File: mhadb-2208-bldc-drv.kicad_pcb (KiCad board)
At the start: 2 copper layers, 45 x 40 mm, 69 parts, among them J1 TC2030, J2 Conn_01x04, J3 Conn_01x04_Pin, M1 Motor_3_Phases, SW1 SW_Push, SW2 SW_Push, SW3 SW_Push, U1 SN65HVD230, U2 STM32F103C8Tx, U3 DRV8311H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

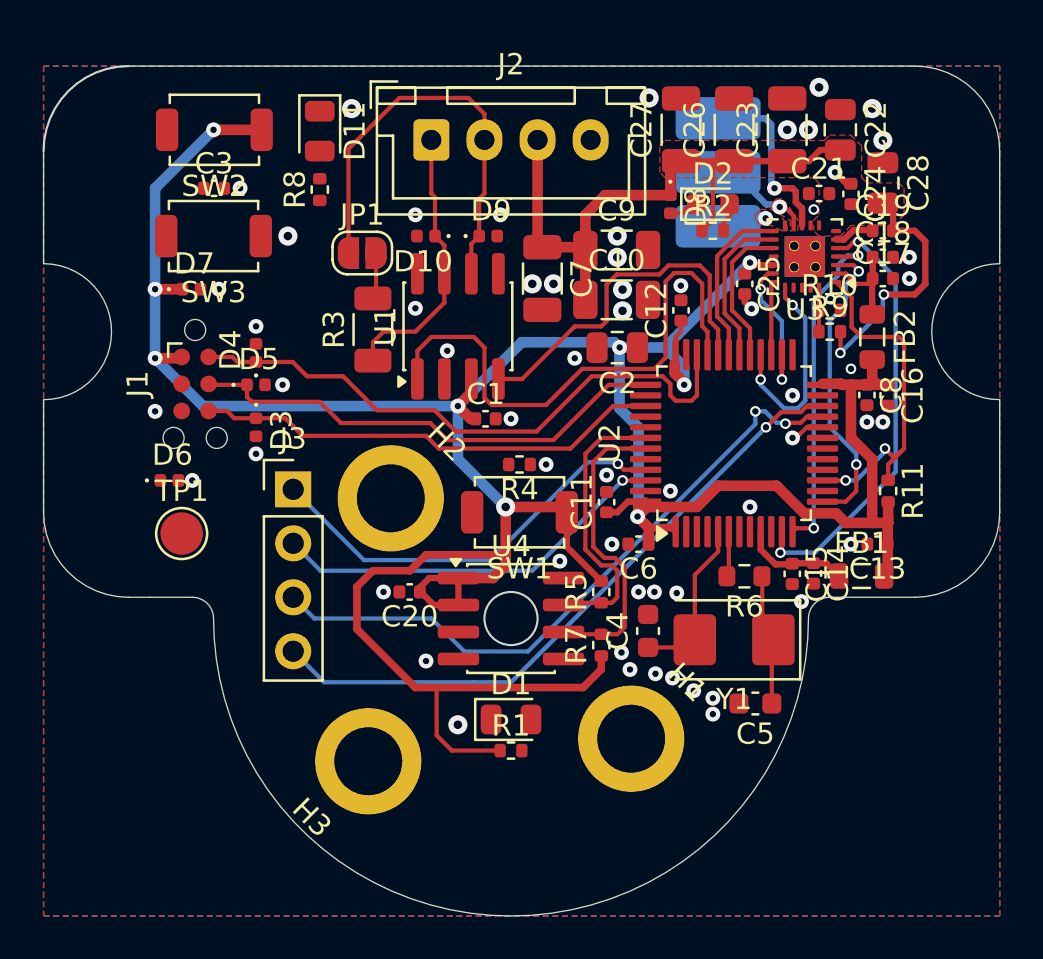
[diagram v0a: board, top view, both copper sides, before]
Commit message: pcb: route BOOT and RST
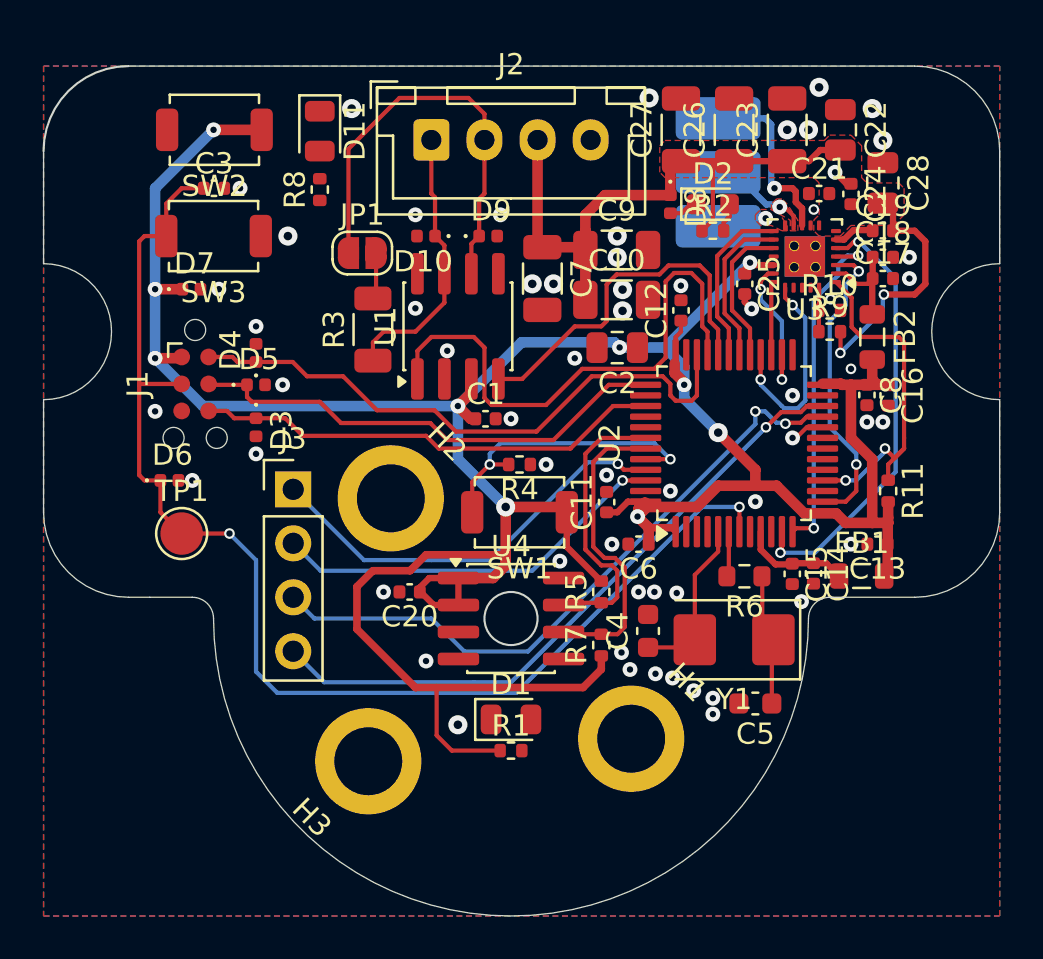
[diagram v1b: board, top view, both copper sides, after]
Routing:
- net /NRST: track 0.00 -> 59.2 mm, vias 0 -> 2
- net /BOOT: track 0.00 -> 14.2 mm, vias 0 -> 2
- net +3V3: track 152.4 -> 150.3 mm, vias 9 -> 10

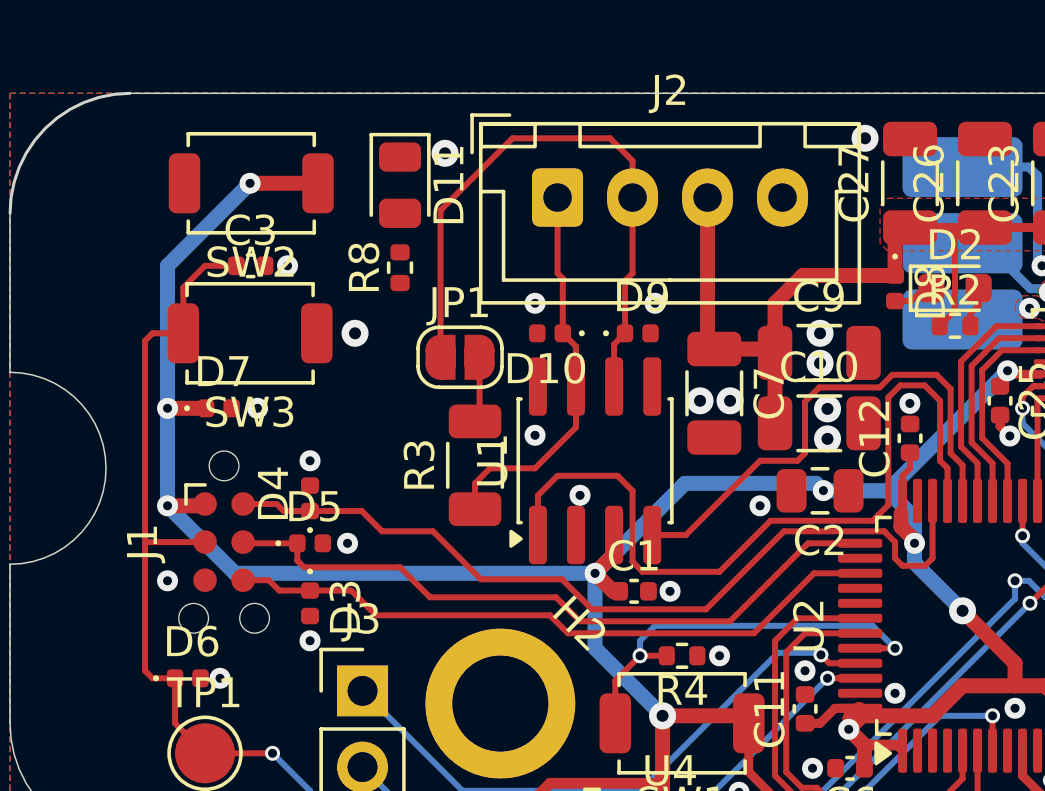
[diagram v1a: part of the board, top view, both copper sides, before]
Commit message: pcb: route BTN and CAN status
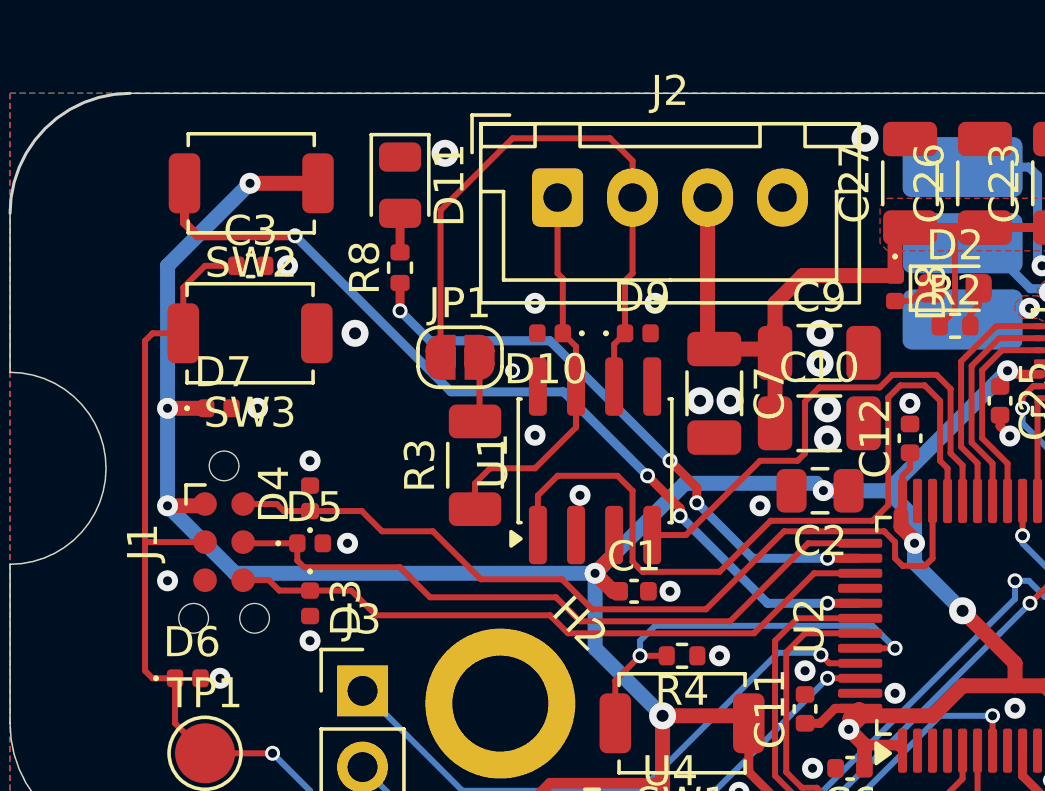
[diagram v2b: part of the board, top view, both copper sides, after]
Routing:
- net /BTN1: track 0.00 -> 29.2 mm, vias 0 -> 4
- net Net-(U2-PA15): track 0.00 -> 20.0 mm, vias 0 -> 4
- net Net-(D11-A): track 0.00 -> 1.30 mm
- net GND: vias 60 -> 61
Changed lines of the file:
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@@
 	)
 	(via
+		(at 113.75 69.25)
+		(size 0.5)
+		(drill 0.3)
+		(layers "F.Cu" "B.Cu")
+		(free yes)
+		(net 2)
+	)
+	(via
 		(at 126.994467 70.337148)
 		(size 0.7)
@@
 	)
 	(segment
+		(start 110 65.3025)
+		(end 110 64)
+		(width 0.3)
+		(layer "F.Cu")
+		(net 15)
+	)
+	(segment
 		(start 129.01 67.353797)
 		(end 129.2875 67.076297)
@@
 	)
 	(segment
+		(start 119.892894 73.142894)
+		(end 119 72.25)
+		(width 0.3)
+		(layer "F.Cu")
+		(net 33)
+	)
+	(segment
+		(start 124.25 75.5)
+		(end 125.3375 75.5)
+		(width 0.3)
+		(layer "F.Cu")
+		(net 33)
+	)
+	(segment
+		(start 119.892894 73.649999)
+		(end 119.892894 73.142894)
+		(width 0.3)
+		(layer "F.Cu")
+		(net 33)
+	)
+	(segment
+		(start 110 66.3225)
+		(end 110 67.25)
+		(width 0.3)
+		(layer "F.Cu")
+		(net 33)
+	)
+	(via
+		(at 119 72.25)
+		(size 0.5)
+		(drill 0.3)
+		(layers "F.Cu" "B.Cu")
+		(net 33)
+	)
+	(via
+		(at 124.25 75.5)
+		(size 0.5)
+		(drill 0.3)
+		(layers "F.Cu" "B.Cu")
+		(net 33)
+	)
+	(via
+		(at 110 67.25)
+		(size 0.5)
+		(drill 0.3)
+		(layers "F.Cu" "B.Cu")
+		(net 33)
+	)
+	(via
+		(at 119.892894 73.649999)
+		(size 0.5)
+		(drill 0.3)
+		(layers "F.Cu" "B.Cu")
+		(net 33)
+	)
+	(segment
+		(start 121.75 75.5)
+		(end 124.25 75.5)
+		(width 0.3)
+		(layer "B.Cu")
+		(net 33)
+	)
+	(segment
+		(start 119.899999 73.649999)
+		(end 121.75 75.5)
+		(width 0.3)
+		(layer "B.Cu")
+		(net 33)
+	)
+	(segment
+		(start 115 68.25)
+		(end 111 68.25)
+		(width 0.3)
+		(layer "B.Cu")
+		(net 33)
+	)
+	(segment
+		(start 119.892894 73.649999)
+		(end 119.899999 73.649999)
+		(width 0.3)
+		(layer "B.Cu")
+		(net 33)
+	)
+	(segment
+		(start 111 68.25)
+		(end 110 67.25)
+		(width 0.3)
+		(layer "B.Cu")
+		(net 33)
+	)
+	(segment
+		(start 119 72.25)
+		(end 115 68.25)
+		(width 0.3)
+		(layer "B.Cu")
+		(net 33)
+	)
+	(segment
 		(start 125.989447 69.804929)
 		(end 123.972972 69.804929)
@@
 	)
 	(segment
+		(start 124.25 77)
+		(end 125.3375 77)
+		(width 0.3)
+		(layer "F.Cu")
+		(net 39)
+	)
+	(segment
+		(start 119.33462 73.83462)
+		(end 119.33462 74.08462)
+		(width 0.3)
+		(layer "F.Cu")
+		(net 39)
+	)
+	(segment
+		(start 102.815 63)
+		(end 102.815 64.315)
+		(width 0.3)
+		(layer "F.Cu")
+		(net 39)
+	)
+	(segment
+		(start 103.25 64.75)
+		(end 106.5 64.75)
+		(width 0.3)
+		(layer "F.Cu")
+		(net 39)
+	)
+	(segment
+		(start 102.815 64.315)
+		(end 103.25 64.75)
+		(width 0.3)
+		(layer "F.Cu")
+		(net 39)
+	)
+	(segment
+		(start 118.25 72.75)
+		(end 119.33462 73.83462)
+		(width 0.3)
+		(layer "F.Cu")
+		(net 39)
+	)
+	(via
+		(at 124.25 77)
+		(size 0.5)
+		(drill 0.3)
+		(layers "F.Cu" "B.Cu")
+		(net 39)
+	)
+	(via
+		(at 118.25 72.75)
+		(size 0.5)
+		(drill 0.3)
+		(layers "F.Cu" "B.Cu")
+		(net 39)
+	)
+	(via
+		(at 106.5 64.75)
+		(size 0.5)
+		(drill 0.3)
+		(layers "F.Cu" "B.Cu")
+		(net 39)
+	)
+	(via
+		(at 119.33462 74.08462)
+		(size 0.5)
+		(drill 0.3)
+		(layers "F.Cu" "B.Cu")
+		(net 39)
+	)
+	(segment
+		(start 115.451 69.951)
+		(end 118.25 72.75)
+		(width 0.3)
+		(layer "B.Cu")
+		(net 39)
+	)
+	(segment
+		(start 106.5 64.75)
+		(end 111.701 69.951)
+		(width 0.3)
+		(layer "B.Cu")
+		(net 39)
+	)
+	(segment
+		(start 122.25 77)
+		(end 124.25 77)
+		(width 0.3)
+		(layer "B.Cu")
+		(net 39)
+	)
+	(segment
+		(start 119.33462 74.08462)
+		(end 122.25 77)
+		(width 0.3)
+		(layer "B.Cu")
+		(net 39)
+	)
+	(segment
+		(start 111.701 69.951)
+		(end 115.451 69.951)
+		(width 0.3)
+		(layer "B.Cu")
+		(net 39)
+	)
+	(segment

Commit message: pcb: add stitching vias
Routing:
- net GND: track 4.91 -> 13.0 mm, vias 61 -> 115
- net Net-(D1-A): track 0.00 -> 1.64 mm
- net +3V3: track 150.3 -> 151.3 mm

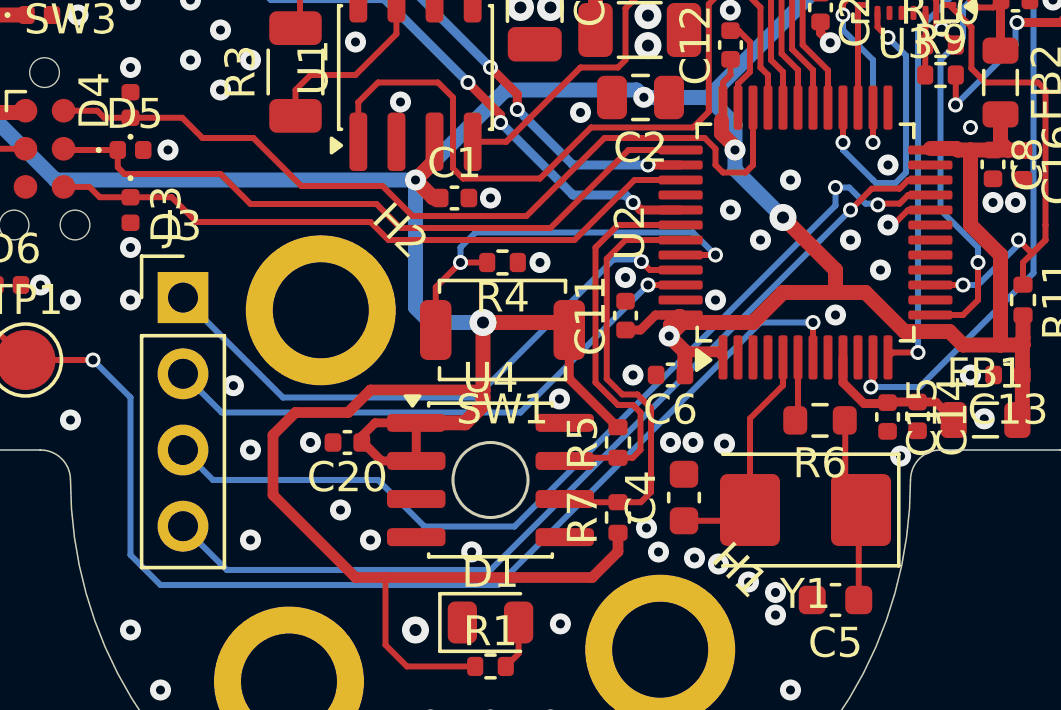
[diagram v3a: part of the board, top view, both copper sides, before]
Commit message: pcb: run and fix DRC
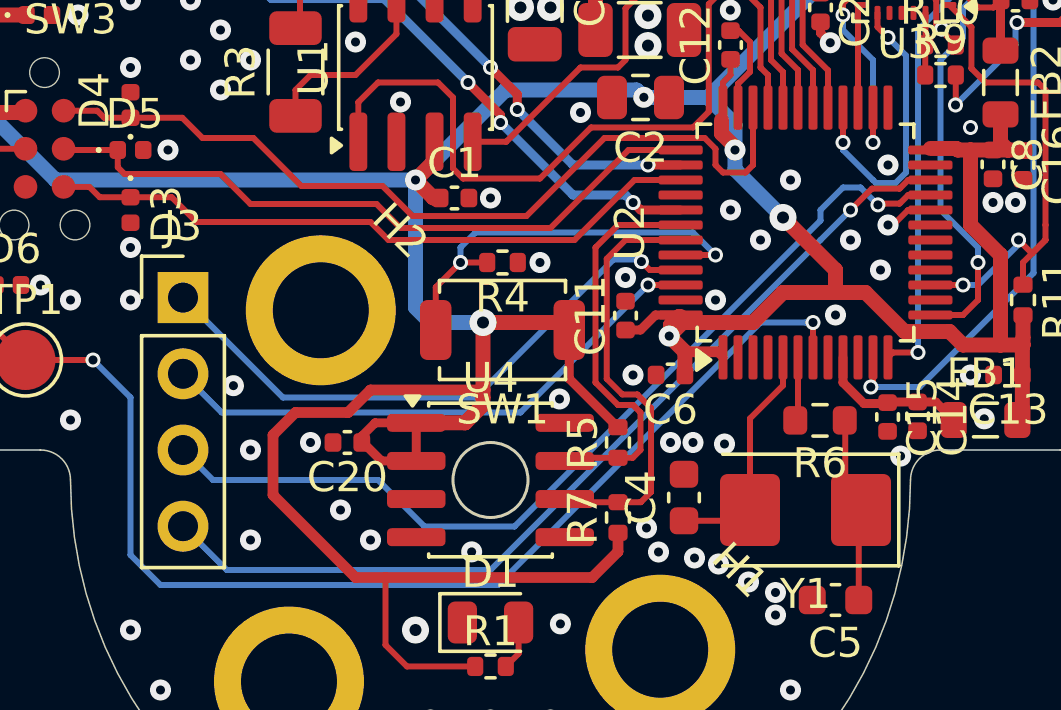
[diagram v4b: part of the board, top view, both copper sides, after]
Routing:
- net Net-(J3-Pin_3): track 31.4 -> 31.2 mm, vias 2 -> 1
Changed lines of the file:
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@@
-	)
-	(via
-		(at 130.5 76.25)
-		(size 0.5)
-		(drill 0.3)
-		(layers "F.Cu" "B.Cu")
-		(net 21)
 	)
 	(via
@@
 	)
 	(segment
-		(start 131.496409 76.787888)
-		(end 131.8733 76.787888)
+		(start 130 77.349943)
+		(end 130 77)
 		(width 0.2)
 		(layer "B.Cu")
@@
 	)
 	(segment
-		(start 130.958521 76.25)
-		(end 131.496409 76.787888)
+		(start 130 77)
+		(end 130.75 76.25)
 		(width 0.2)
 		(layer "B.Cu")
@@
 	)
 	(segment
-		(start 131.8733 76.787888)
+		(start 109.75 86)
+		(end 115.25 86)
+		(width 0.2)
+		(layer "B.Cu")
+		(net 21)
+	)
+	(segment
+		(start 108.75 85)
+		(end 109.75 86)
+		(width 0.2)
+		(layer "B.Cu")
+		(net 21)
+	)
+	(segment
+		(start 116.801 87.551)
+		(end 119.798943 87.551)
+		(width 0.2)
+		(layer "B.Cu")
+		(net 21)
+	)
+	(segment
+		(start 119.798943 87.551)
+		(end 130 77.349943)
+		(width 0.2)
+		(layer "B.Cu")
+		(net 21)
+	)
+	(segment
+		(start 131.335412 76.25)
 		(end 131.914589 76.829177)
 		(width 0.2)
@@
 	(segment
 		(start 115.25 86)
-		(end 109.75 86)
+		(end 116.801 87.551)
 		(width 0.2)
 		(layer "B.Cu")
@@
 	)
 	(segment
-		(start 116.801 87.551)
-		(end 115.25 86)
+		(start 130.75 76.25)
+		(end 131.335412 76.25)
 		(width 0.2)
 		(layer "B.Cu")
-		(net 21)
-	)
-	(segment
-		(start 130.5 76.849943)
-		(end 119.798943 87.551)
-		(width 0.2)
-		(layer "B.Cu")
-		(net 21)
-	)
-	(segment
-		(start 130.5 76.25)
-		(end 130.958521 76.25)
-		(width 0.2)
-		(layer "B.Cu")
-		(net 21)
-	)
-	(segment
-		(start 109.75 86)
-		(end 108.75 85)
-		(width 0.2)
-		(layer "B.Cu")
-		(net 21)
-	)
-	(segment
-		(start 130.5 76.25)
-		(end 130.5 76.849943)
-		(width 0.2)
-		(layer "B.Cu")
-		(net 21)
-	)
-	(segment
-		(start 119.798943 87.551)
-		(end 116.801 87.551)
-		(width 0.2)
-		(layer "B.Cu")
